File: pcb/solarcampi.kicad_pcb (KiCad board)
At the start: 2 copper layers, 65 x 30 mm, 30 parts, among them J2 Vin 12V, J3 AVR-ISP-6, Q1 IRLML 2244, Q2 BCR 108 SMD, U1 INA226, U2 ATmega328P-AU, U3 TPS71533__SC70

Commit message: Layout RevB
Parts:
- removed the C3 at (59.4, 61.7)
- removed the C8 at (80.2, 57.8)
- removed G***: LOGO, StudioPieters:StudioPieters_Kicad_Logo
- removed the Q2 at (88.4, 70.9)
- removed TGT_PWR: Jumper_2_Open, Jumper:SolderJumper-2_P1.3mm_Open_Pad1.0x1.5mm
- removed the U3 at (61.9, 61.4)
- added C2: 100n, Capacitor_SMD:C_0805_2012Metric_Pad1.15x1.40mm_HandSolder, B.Cu at (84.2, 64.3)
- added C6: C, Capacitor_SMD:C_0805_2012Metric_Pad1.15x1.40mm_HandSolder, F.Cu at (77.2, 76.0)
- added D1: D, Diode_SMD:D_SOD-123, F.Cu at (60.3, 62.1)
- added D2: LED, LED_SMD:LED_0805_2012Metric_Pad1.15x1.40mm_HandSolder, F.Cu at (102.0, 67.3)
- added D3: D_Zener, Diode_SMD:D_SOD-123, F.Cu at (77.5, 59.1)
- added F2: Fuse, Fuse:Fuse_0805_2012Metric_Pad1.15x1.40mm_HandSolder, F.Cu at (80.7, 60.8)
- added J3: FTDI_AVR, Connector_PinHeader_2.54mm:PinHeader_1x06_P2.54mm_Vertical, F.Cu at (109.5, 57.7)
- added JP2: Jumper_NO_Small, Connector_PinHeader_2.54mm:PinHeader_1x02_P2.54mm_Vertical, F.Cu at (88.4, 76.9)
- added JP3: Jumper_NO_Small, Jumper:SolderJumper-2_P1.3mm_Open_Pad1.0x1.5mm, F.Cu at (91.2, 57.6)
- added JP4: Jumper_NO_Small, Jumper:SolderJumper-2_P1.3mm_Open_Pad1.0x1.5mm, F.Cu at (94.1, 57.6)
- added JP5: Jumper_NO_Small, Jumper:SolderJumper-2_P1.3mm_Open_Pad1.0x1.5mm, F.Cu at (97.0, 57.6)
- added Q1: Q_NMOS_GDS, Package_TO_SOT_SMD:SOT-23, F.Cu at (85.0, 70.5)
- added Q3: Q_NMOS_GDS, Package_TO_SOT_SMD:SOT-23, F.Cu at (73.8, 70.7)
- added Q4: Q_NMOS_GDS, Package_TO_SOT_SMD:SOT-23, B.Cu at (104.7, 74.2)
- added R2: R, Resistor_SMD:R_0805_2012Metric_Pad1.15x1.40mm_HandSolder, F.Cu at (105.9, 66.3)
- added R6: 1M, Resistor_SMD:R_0805_2012Metric_Pad1.15x1.40mm_HandSolder, F.Cu at (88.4, 70.4)
- added R7: 1M, Resistor_SMD:R_0805_2012Metric_Pad1.15x1.40mm_HandSolder, B.Cu at (72.6, 67.2)
- added R8: 1M, Resistor_SMD:R_0805_2012Metric_Pad1.15x1.40mm_HandSolder, B.Cu at (104.6, 77.2)
- added TP1: 12V, TestPoint:TestPoint_Pad_1.0x1.0mm, F.Cu at (60.0, 75.8)
- added TP2: 3V3, TestPoint:TestPoint_Pad_1.0x1.0mm, F.Cu at (96.4, 64.9)
- added TP3: 5V, TestPoint:TestPoint_Pad_1.0x1.0mm, F.Cu at (87.6, 57.8)
- added U2: TPS71533__SC70, Package_TO_SOT_SMD:SOT-353_SC-70-5_Handsoldering, B.Cu at (86.8, 64.6)
- C4, R3, R4: moved to B.Cu
- C9: value 100n -> 10µ
- J1: renamed from J2; footprint solarcampi:zweipolige_Anreihklemme -> TerminalBlock:TerminalBlock_bornier-2_P5.08mm
- J5: renamed from FTDI; value FTDI -> FTDI_RPI
- Q2: renamed from Q1; moved to F.Cu
- R5: renamed from R1; value 10k -> 1M
- moved C4 25.8 mm to (89.3, 64.3), turned to 270 degrees
- moved R3 7.69 mm to (79.9, 64.8), turned to 0 degrees
- moved C9 7.45 mm to (73.9, 60.8), turned to 180 degrees
- moved R5 7.23 mm to (77.2, 72.2), turned to 90 degrees
- moved U1 6.75 mm to (78.6, 61.8)
- moved C1 5.33 mm to (76.4, 65.8), turned to 270 degrees
- moved R4 4.84 mm to (79.9, 66.9), turned to 0 degrees
- moved Q2 4.27 mm to (80.8, 72.2), turned to 0 degrees
- moved J5 3.18 mm to (65.7, 57.9)
- moved C3 2.58 mm to (74.2, 62.9)
- moved PS1 2.56 mm to (77.7, 67.0)
- moved F1 1.76 mm to (56.1, 70.1)
- moved C5 0.94 mm to (95.4, 62.6), turned to 180 degrees
- renumbered C5 to C1, C1 to C3, C7 to C5, C2 to C7, C6 to C8, J3 to J2, RPI to J4, R2 to R1, U2 to U3
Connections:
- C9 pad 1: /AVR_I2C_PULLUP -> Net-(C9-Pad1)
- J4 pad 11: Net-(J1-Pad11) -> /RST
- J4 pad 13: Net-(J1-Pad13) -> /PWR_OVR
- J4 pad 2: /RPI_5V -> Net-(C9-Pad1)
- R3 pad 1: /AVR_SCL -> /AVR_SDA
- R3 pad 2: /AVR_I2C_PULLUP -> /INA_3V3
- R4 pad 1: /AVR_SDA -> /AVR_SCL
- R4 pad 2: /AVR_I2C_PULLUP -> /INA_3V3
- U3 pad 19: /AVR_I2C_PULLUP -> Net-(U3-Pad19)
- U3 pad 22: /AVR_SCL -> Net-(U3-Pad22)
- U3 pad 23: /AVR_SDA -> /AVR_SCL
- U3 pad 24: /INA_3V3 -> /AVR_SDA
- U3 pad 25: Net-(U2-Pad25) -> /INA_3V3
- U3 pad 30: Net-(U2-Pad30) -> /RXD
- U3 pad 31: Net-(U2-Pad31) -> /TXD
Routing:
- net /RST: track 0.00 -> 73.3 mm
- net +3V3: track 67.0 -> 30.1 mm, vias 2 -> 1
- net Net-(C9-Pad1): track 0.00 -> 28.3 mm, vias 0 -> 3
- net /RPI_5V: track 36.2 -> 8.87 mm, vias 1 -> 0
- net /RXD: track 0.00 -> 24.8 mm
- net /PWR_OVR: track 0.00 -> 21.9 mm, vias 0 -> 2
- net /TXD: track 0.00 -> 18.2 mm
- net Net-(JP2-Pad2): track 4.70 -> 21.9 mm, vias 1 -> 2
- net /AVR_I2C_PULLUP: track 14.1 -> 0.00 mm, vias 1 -> 0
- net /MOSI: track 7.39 -> 19.7 mm, vias 0 -> 1
- net Net-(J4-Pad23): track 0.00 -> 11.9 mm
- net +12V: track 63.7 -> 75.6 mm, vias 3 -> 4
- net Net-(J4-Pad21): track 0.00 -> 11.6 mm
- net Net-(J4-Pad19): track 0.00 -> 11.3 mm
- net /MISO: track 10.0 -> 20.9 mm, vias 0 -> 3
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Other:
- board text added: "+"
- board text added: "+12V"
- board text added: "+3V3"
- board text added: "+5V"
- board text added: "AVR"
- board text added: "GND"
- board text added: "RPI"
- board text added: "SolarCamPi RevB"
- board text removed: "SolarCamPi RevA"

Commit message: Add 2-pin screw terminal with 3d model
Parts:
- J1: footprint TerminalBlock:TerminalBlock_bornier-2_P5.08mm -> solarcampi:TerminalBlock_bornier-2_P5.08mm
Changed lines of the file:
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@@
     (add_net "Net-(U3-Pad8)")
+  )
+  (module solarcampi:TerminalBlock_bornier-2_P5.08mm (layer F.Cu)
+    (at 54.102 59.182 270)
+    (descr "simple 2-pin terminal block, pitch 5.08mm, revamped version of bornier2")
+    (tags "terminal block bornier2")
+    (fp_text reference J1 (at -1.182 -5.398 180) (layer F.SilkS)
+      (effects (font (size 1 1) (thickness 0.15)))
+    )
+    (fp_text value "Vin 12V" (at 2.54 5.08 90) (layer F.Fab)
+      (effects (font (size 1 1) (thickness 0.15)))
+    )
+    (fp_line (start 7.79 4) (end -2.71 4) (layer F.CrtYd) (width 0.05))
+    (fp_line (start 7.79 4) (end 7.79 -4) (layer F.CrtYd) (width 0.05))
+    (fp_line (start -2.71 -4) (end -2.71 4) (layer F.CrtYd) (width 0.05))
+    (fp_line (start -2.71 -4) (end 7.79 -4) (layer F.CrtYd) (width 0.05))
+    (fp_line (start -2.54 3.81) (end 7.62 3.81) (layer F.SilkS) (width 0.12))
+    (fp_line (start -2.54 -3.81) (end -2.54 3.81) (layer F.SilkS) (width 0.12))
+    (fp_line (start 7.62 -3.81) (end -2.54 -3.81) (layer F.SilkS) (width 0.12))
+    (fp_line (start 7.62 3.81) (end 7.62 -3.81) (layer F.SilkS) (width 0.12))
+    (fp_line (start 7.62 2.54) (end -2.54 2.54) (layer F.SilkS) (width 0.12))
+    (fp_line (start 7.54 -3.75) (end -2.46 -3.75) (layer F.Fab) (width 0.1))
+    (fp_line (start 7.54 3.75) (end 7.54 -3.75) (layer F.Fab) (width 0.1))
+    (fp_line (start -2.46 3.75) (end 7.54 3.75) (layer F.Fab) (width 0.1))
+    (fp_line (start -2.46 -3.75) (end -2.46 3.75) (layer F.Fab) (width 0.1))
+    (fp_line (start -2.41 2.55) (end 7.49 2.55) (layer F.Fab) (width 0.1))
+    (fp_text user %R (at 2.54 0 90) (layer F.Fab)
+      (effects (font (size 1 1) (thickness 0.15)))
+    )
+    (pad 2 thru_hole circle (at 5.08 0 270) (size 3 3) (drill 1.52) (layers *.Cu *.Mask)
+      (net 6 "Net-(F1-Pad2)"))
+    (pad 1 thru_hole rect (at 0 0 270) (size 3 3) (drill 1.52) (layers *.Cu *.Mask)
+      (net 1 GND))
+    (model ${KIPRJMOD}/lib/3d/DG340-3.81-02P-12-00AH.STEP
+      (offset (xyz -2.55 0.55 5.63))
+      (scale (xyz 1.34 1.34 1.34))
+      (rotate (xyz -90 0 0))
+    )
   )
   (module Connector_PinHeader_2.54mm:PinHeader_1x02_P2.54mm_Vertical (layer F.Cu)
@@
       (scale (xyz 1 1 1))
       (rotate (xyz 0 0 0))
-    )
-  )
-  (module TerminalBlock:TerminalBlock_bornier-2_P5.08mm (layer F.Cu)
-    (at 54.102 59.182 270)
-    (descr "simple 2-pin terminal block, pitch 5.08mm, revamped version of bornier2")
-    (tags "terminal block bornier2")
-    (fp_text reference J1 (at -1.182 -5.398 180) (layer F.SilkS)
-      (effects (font (size 1 1) (thickness 0.15)))
-    )
-    (fp_text value "Vin 12V" (at 2.54 5.08 90) (layer F.Fab)
-      (effects (font (size 1 1) (thickness 0.15)))
-    )
-    (fp_line (start 7.79 4) (end -2.71 4) (layer F.CrtYd) (width 0.05))
-    (fp_line (start 7.79 4) (end 7.79 -4) (layer F.CrtYd) (width 0.05))
-    (fp_line (start -2.71 -4) (end -2.71 4) (layer F.CrtYd) (width 0.05))
-    (fp_line (start -2.71 -4) (end 7.79 -4) (layer F.CrtYd) (width 0.05))
-    (fp_line (start -2.54 3.81) (end 7.62 3.81) (layer F.SilkS) (width 0.12))
-    (fp_line (start -2.54 -3.81) (end -2.54 3.81) (layer F.SilkS) (width 0.12))
-    (fp_line (start 7.62 -3.81) (end -2.54 -3.81) (layer F.SilkS) (width 0.12))
-    (fp_line (start 7.62 3.81) (end 7.62 -3.81) (layer F.SilkS) (width 0.12))
-    (fp_line (start 7.62 2.54) (end -2.54 2.54) (layer F.SilkS) (width 0.12))
-    (fp_line (start 7.54 -3.75) (end -2.46 -3.75) (layer F.Fab) (width 0.1))
-    (fp_line (start 7.54 3.75) (end 7.54 -3.75) (layer F.Fab) (width 0.1))
-    (fp_line (start -2.46 3.75) (end 7.54 3.75) (layer F.Fab) (width 0.1))
-    (fp_line (start -2.46 -3.75) (end -2.46 3.75) (layer F.Fab) (width 0.1))
-    (fp_line (start -2.41 2.55) (end 7.49 2.55) (layer F.Fab) (width 0.1))
-    (fp_text user %R (at 2.54 0 90) (layer F.Fab)
-      (effects (font (size 1 1) (thickness 0.15)))
-    )
-    (pad 2 thru_hole circle (at 5.08 0 270) (size 3 3) (drill 1.52) (layers *.Cu *.Mask)
-      (net 6 "Net-(F1-Pad2)"))
-    (pad 1 thru_hole rect (at 0 0 270) (size 3 3) (drill 1.52) (layers *.Cu *.Mask)
-      (net 1 GND))
-    (model ${KISYS3DMOD}/TerminalBlock.3dshapes/TerminalBlock_bornier-2_P5.08mm.wrl
-      (offset (xyz 2.539999961853027 0 0))
-      (scale (xyz 1 1 1))
-      (rotate (xyz 0 0 0))

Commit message: Minor aesthetic fixups
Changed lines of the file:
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@@
     (effects (font (size 1.5 1.5) (thickness 0.3)) (justify right mirror))
   )
-  (gr_text "SolarCamPi\nRevB\n" (at 104.9 61.5) (layer F.SilkS)
+  (gr_text "SolarCamPi\nRevB\n" (at 103.6 61.5) (layer F.SilkS)
     (effects (font (size 1.5 1.5) (thickness 0.3)) (justify right))
   )

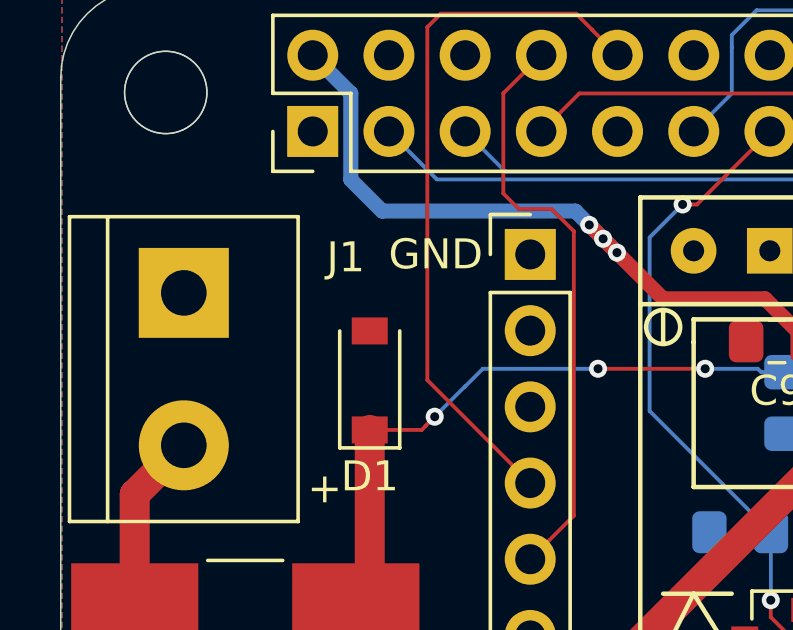
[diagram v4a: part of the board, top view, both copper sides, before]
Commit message: Add more GND pins to reduce GND loop area
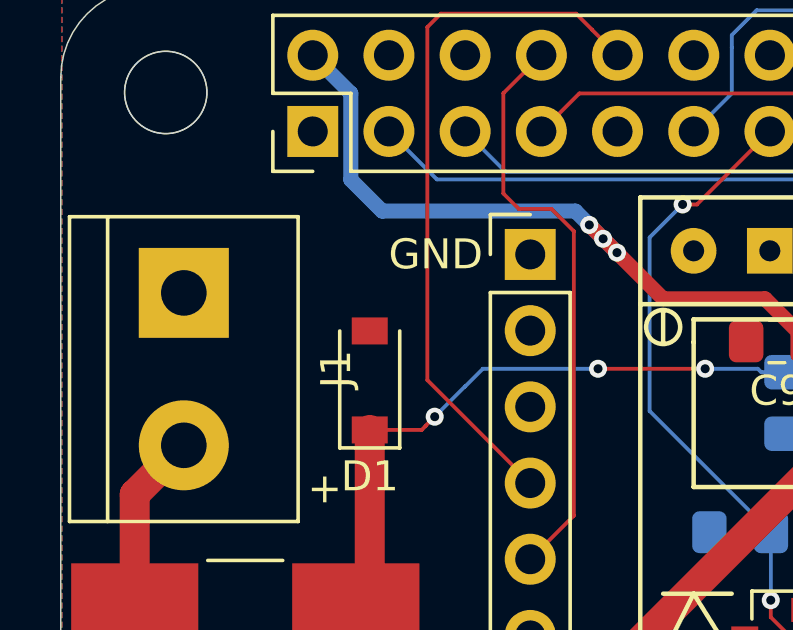
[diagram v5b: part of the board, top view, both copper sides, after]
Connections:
- J4 pad 9: Net-(J4-Pad9) -> GND

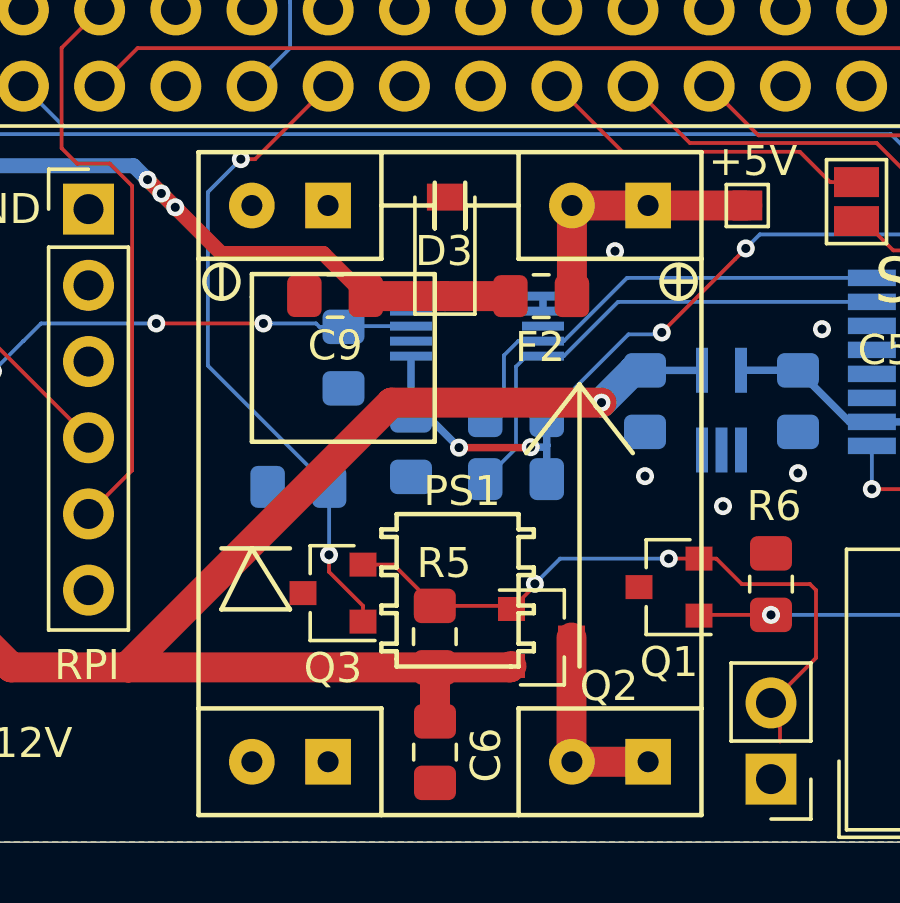
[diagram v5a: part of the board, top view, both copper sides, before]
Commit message: Widen throughholes for regulator footprint to 1 mm
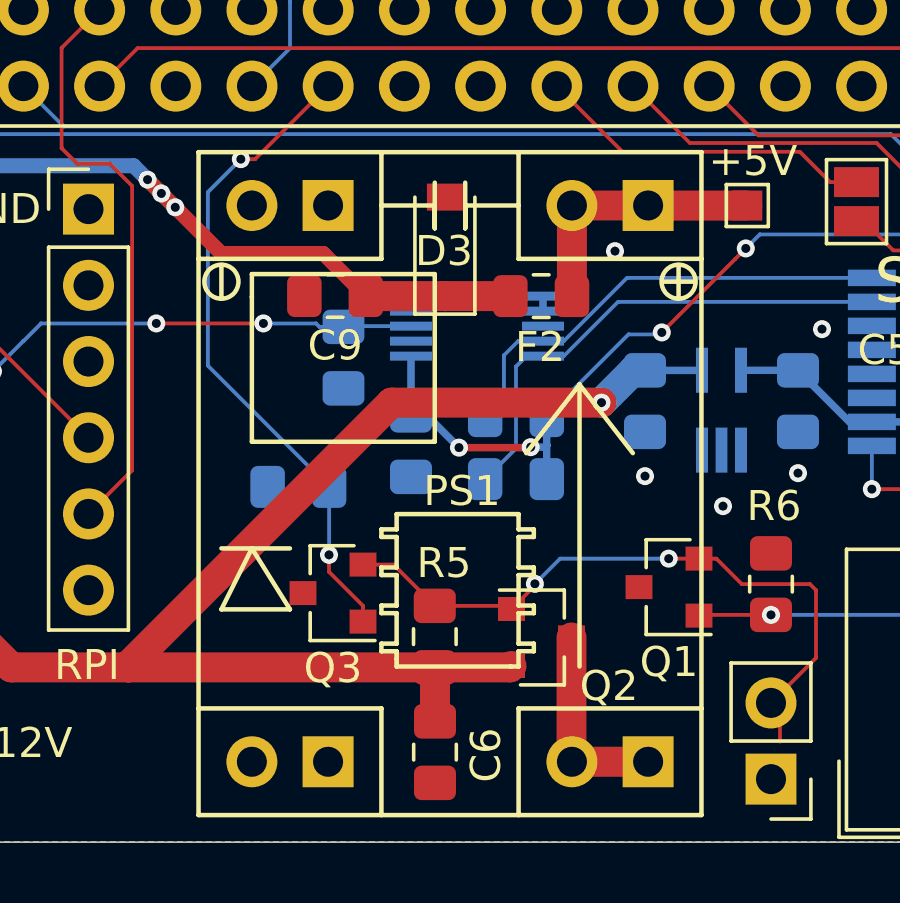
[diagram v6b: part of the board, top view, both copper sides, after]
